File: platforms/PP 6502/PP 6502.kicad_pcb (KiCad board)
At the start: 2 copper layers, 99.1 x 99.1 mm, 21 parts, among them J1 Signals, J3 SBC, J4 ADDRESS, J5 Port A, J6 Port B, J7 PWR1, J8 PWR2, M1 Mounting, M2 Mounting, M3 Mounting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

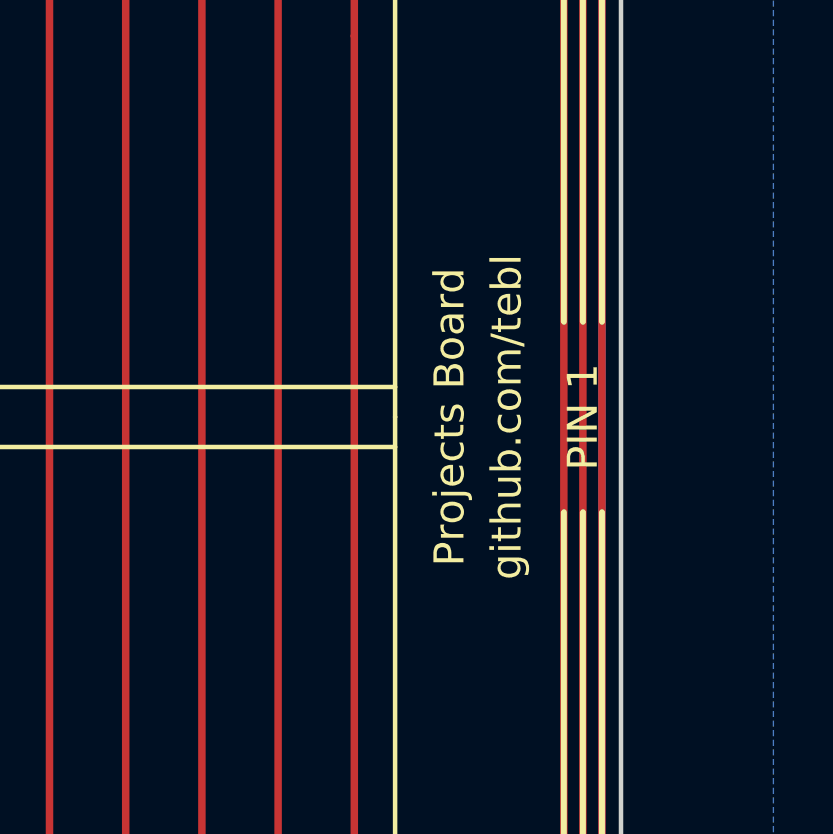
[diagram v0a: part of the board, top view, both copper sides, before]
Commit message: Moved into this repository
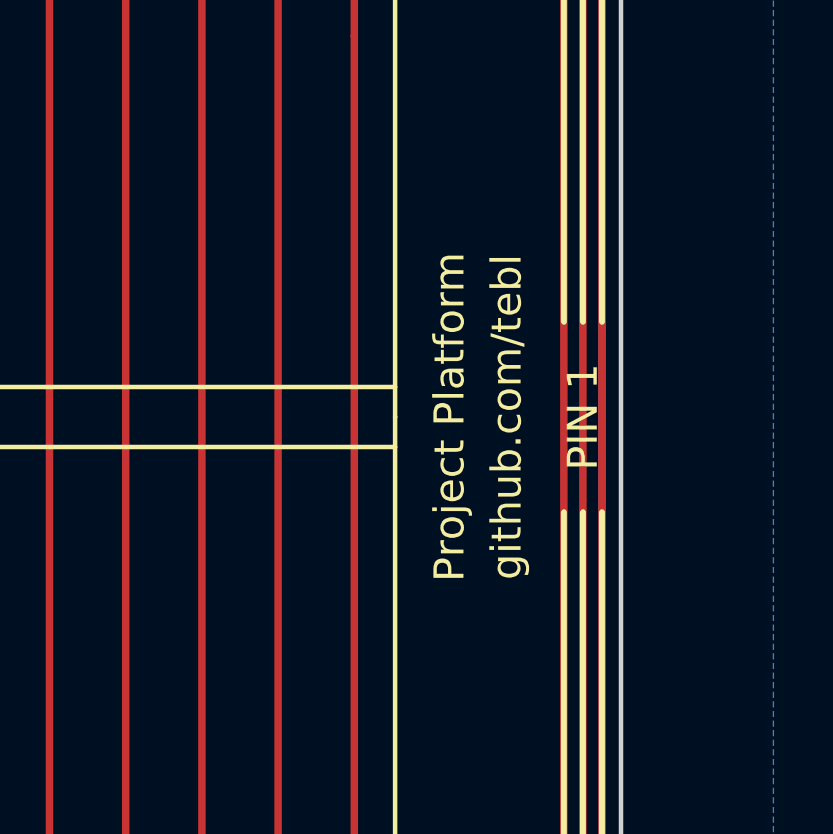
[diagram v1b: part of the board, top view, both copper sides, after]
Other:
- board text added: "Project Platform"
- board text removed: "Projects Board"
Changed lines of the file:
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@@
     (links 121)
     (no_connects 0)
-    (area 100.254999 48.184999 199.465001 147.395001)
+    (area 93.345 43.815 204.470001 161.290001)
     (thickness 1.6)
     (drawings 463)
@@
     (effects (font (size 1 1) (thickness 0.15)))
   )
-  (gr_text "Projects Board" (at 193.675 109.855 90) (layer F.SilkS)
+  (gr_text "Project Platform" (at 193.675 109.855 90) (layer F.SilkS)
     (effects (font (size 1 1) (thickness 0.15)))
   )

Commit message: Silkscreen tweaks
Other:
- board text added: "$1700"
- board text added: "- $170F"
- board text added: "IO3"
- board text added: "RDY"
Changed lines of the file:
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@@
     (links 121)
     (no_connects 0)
-    (area 93.345 43.815 204.470001 161.290001)
+    (area 100.254999 48.184999 199.465001 147.395001)
     (thickness 1.6)
-    (drawings 463)
+    (drawings 471)
     (tracks 663)
     (zones 0)
@@
     (descr "Through hole straight pin header, 1x03, 2.54mm pitch, single row")
     (tags "Through hole pin header THT 1x03 2.54mm single row")
-    (fp_text reference JP3 (at 0 -2.33 90) (layer F.SilkS)
+    (fp_text reference JP3 (at 0 -2.54 90) (layer F.Fab)
       (effects (font (size 1 1) (thickness 0.15)))
     )
@@
       (rotate (xyz 0 0 0))
     )
+  )
+  (gr_line (start 161.29 88.265) (end 161.925 88.9) (angle 90) (layer B.SilkS) (width 0.2))
+  (gr_line (start 161.29 62.23) (end 161.29 88.265) (angle 90) (layer B.SilkS) (width 0.2))
+  (gr_line (start 160.655 61.595) (end 161.29 62.23) (angle 90) (layer B.SilkS) (width 0.2))
+  (gr_line (start 159.385 61.595) (end 160.655 61.595) (angle 90) (layer B.SilkS) (width 0.2))
+  (gr_line (start 170.815 88.9) (end 161.925 88.9) (angle 90) (layer B.SilkS) (width 0.2))
+  (gr_text IO3 (at 182.88 88.9) (layer B.SilkS)
+    (effects (font (size 0.8 0.8) (thickness 0.1)) (justify mirror))
+  )
+  (gr_text "- $170F" (at 173.99 88.9) (layer B.SilkS)
+    (effects (font (size 0.8 0.8) (thickness 0.1)) (justify mirror))
+  )
+  (gr_text $1700 (at 179.07 88.9) (layer B.SilkS)
+    (effects (font (size 0.8 0.8) (thickness 0.1)) (justify mirror))
   )
   (gr_line (start 132.715 59.055) (end 141.605 59.055) (angle 90) (layer B.SilkS) (width 0.2))
@@
     (effects (font (size 1 1) (thickness 0.15)) (justify left))
   )
-  (gr_text READY (at 137.16 52.705 270) (layer F.SilkS)
+  (gr_text RDY (at 137.16 52.705 270) (layer F.SilkS)
     (effects (font (size 1 1) (thickness 0.15)) (justify left))
   )

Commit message: Fixed 6502 address calculations
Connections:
- net /8K1 renamed /4K3
- net /8K2 renamed /4K5
- net /8K3 renamed /4K7
- net /8K4 renamed /4K9
- net /8K5 renamed /4KB
- net /8K6 renamed /4KD
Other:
- board text added: "$3000"
- board text added: "$5000"
- board text added: "$7000"
- board text added: "$9000"
- board text added: "$B000"
- board text added: "$D000"
- board text added: "$xx00"
- board text added: "$xx01"
- board text added: "$xx02"
- board text added: "$xx03"
- board text added: "$xx04"
- board text added: "$xx05"
- board text added: "$xx06"
- board text added: "$xx07"
- board text added: "$xx08"
- board text added: "$xx09"
- board text added: "$xx0A"
- board text added: "$xx0B"
- board text added: "$xx0C"
- board text added: "$xx0D"
- board text added: "$xx0E"
- board text added: "$xx0F"
- board text added: "- $300F"
- board text added: "- $500F"
- board text added: "- $700F"
- board text added: "- $900F"
- board text added: "- $B00F"
- board text added: "- $D00F"
- board text added: "1-2 6502 PHI2"
- board text added: "2-3 6800 E"
- board text added: "4K3"
- board text added: "4K5"
- board text added: "4K7"
- board text added: "4K9"
- board text added: "4KB"
- board text added: "4KD"
- board text removed: "$2000"
- board text removed: "$4000"
- board text removed: "$6000"
- board text removed: "$8000"
- board text removed: "$A000"
- board text removed: "$C000"
- board text removed: "$x000"
- board text removed: "$x001"
- board text removed: "$x002"
- board text removed: "$x003"
- board text removed: "$x004"
- board text removed: "$x005"
- board text removed: "$x006"
- board text removed: "$x007"
- board text removed: "$x008"
- board text removed: "$x009"
- board text removed: "$x00A"
- board text removed: "$x00B"
- board text removed: "$x00C"
- board text removed: "$x00D"
- board text removed: "$x00E"
- board text removed: "$x00F"
- board text removed: "- $200F"
- board text removed: "- $400F"
- board text removed: "- $600F"
- board text removed: "- $800F"
- board text removed: "- $A00F"
- board text removed: "- $C00F"
- board text removed: "8K1"
- board text removed: "8K2"
- board text removed: "8K3"
- board text removed: "8K4"
- board text removed: "8K5"
- board text removed: "8K6"
